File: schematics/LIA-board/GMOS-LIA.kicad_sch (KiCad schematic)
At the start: 0 parts

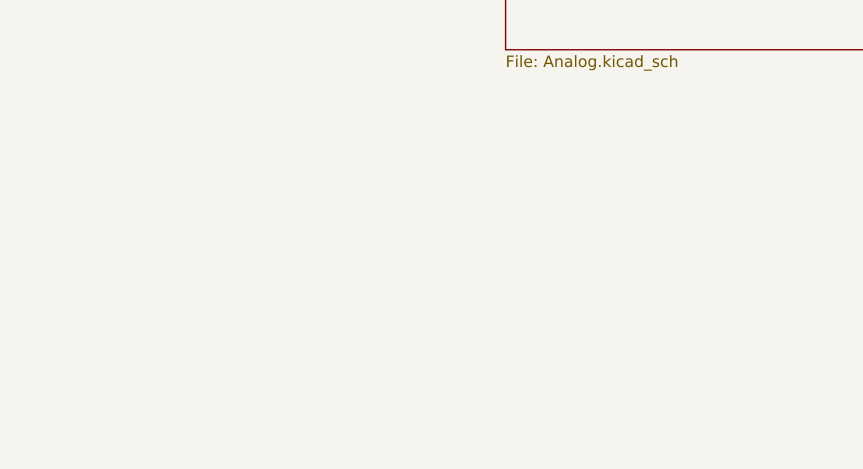
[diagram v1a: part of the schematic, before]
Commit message: some simulations, new page in kicad scematic
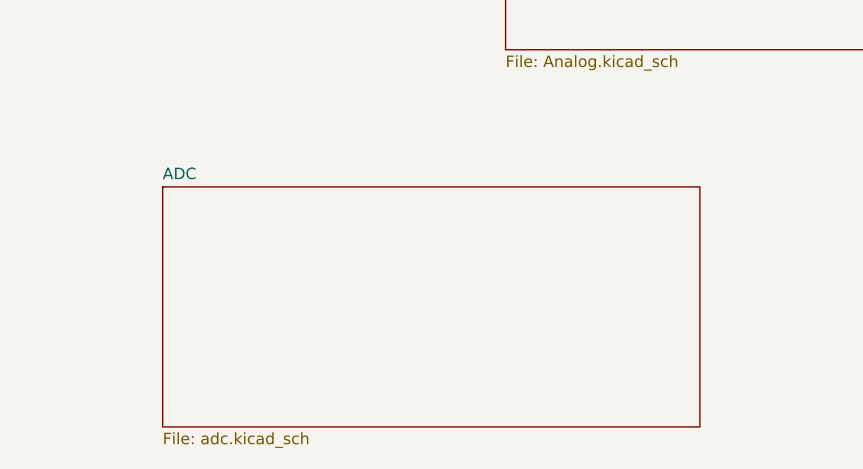
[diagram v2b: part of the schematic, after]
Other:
- added sheet ADC (adc.kicad_sch)
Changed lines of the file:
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@@
+		)
+	)
+	(sheet
+		(at 114.3 116.84)
+		(size 59.69 26.67)
+		(exclude_from_sim no)
+		(in_bom yes)
+		(on_board yes)
+		(dnp no)
+		(fields_autoplaced yes)
+		(stroke
+			(width 0.1524)
+			(type solid)
+		)
+		(fill
+			(color 0 0 0 0)
+		)
+		(property "Sheetname" "ADC"
+			(at 114.3 116.1284 0)
+			(show_name no)
+			(do_not_autoplace no)
+			(effects
+				(font
+					(size 1.27 1.27)
+				)
+				(justify left bottom)
+			)
+		)
+		(property "Sheetfile" "adc.kicad_sch"
+			(at 114.3 144.0946 0)
+			(show_name no)
+			(do_not_autoplace no)
+			(effects
+				(font
+					(size 1.27 1.27)
+				)
+				(justify left top)
+			)
+		)
+		(instances
+			(project "GMOS-LIA"
+				(path "/87b3d1ed-39bd-4cff-a405-e580c48ff0ef"
+					(page "7")
+				)
+			)
 		)
 	)

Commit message: all current changes
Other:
- sheet GMOS_Sock renamed GMOS_MUX
- sheet GMOS_MUX: file GMOS_Sock.kicad_sch -> GMOS_MUX.kicad_sch
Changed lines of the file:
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@@
 			(color 0 0 0 0)
 		)
-		(property "Sheetname" "GMOS_Sock"
+		(property "Sheetname" "GMOS_MUX"
 			(at 38.1 75.4884 0)
 			(show_name no)
@@
 			)
 		)
-		(property "Sheetfile" "GMOS_Sock.kicad_sch"
+		(property "Sheetfile" "GMOS_MUX.kicad_sch"
 			(at 38.1 111.0746 0)
 			(show_name no)

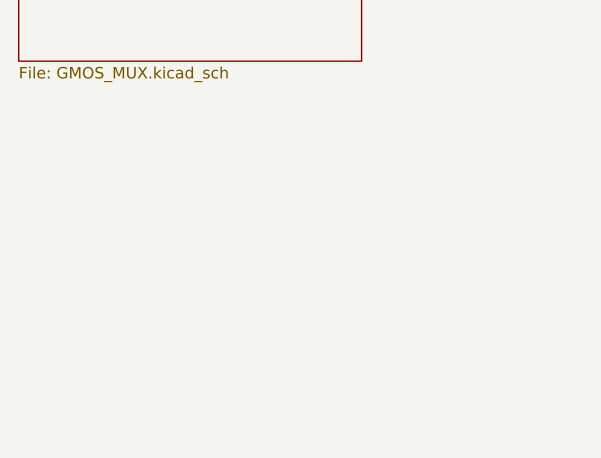
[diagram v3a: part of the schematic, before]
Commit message: added MCU
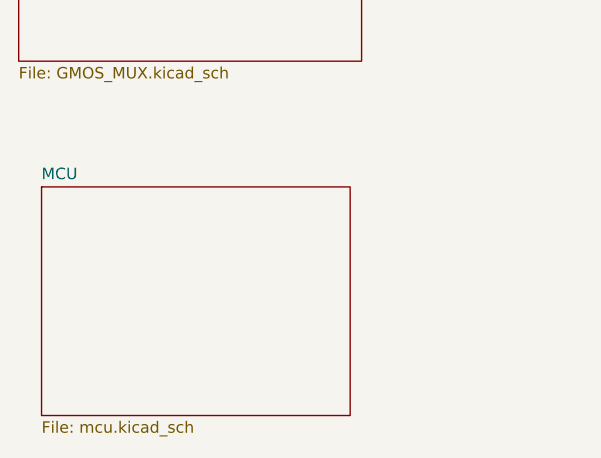
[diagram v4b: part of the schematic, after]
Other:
- added sheet MCU (mcu.kicad_sch)
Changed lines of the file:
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@@
+	)
+	(sheet
+		(at 40.64 124.46)
+		(size 34.29 25.4)
+		(exclude_from_sim no)
+		(in_bom yes)
+		(on_board yes)
+		(dnp no)
+		(fields_autoplaced yes)
+		(stroke
+			(width 0.1524)
+			(type solid)
+		)
+		(fill
+			(color 0 0 0 0)
+		)
+		(property "Sheetname" "MCU"
+			(at 40.64 123.7484 0)
+			(show_name no)
+			(do_not_autoplace no)
+			(effects
+				(font
+					(size 1.27 1.27)
+				)
+				(justify left bottom)
+			)
+		)
+		(property "Sheetfile" "mcu.kicad_sch"
+			(at 40.64 150.4446 0)
+			(show_name no)
+			(do_not_autoplace no)
+			(effects
+				(font
+					(size 1.27 1.27)
+				)
+				(justify left top)
+			)
+		)
+		(instances
+			(project "GMOS-LIA"
+				(path "/87b3d1ed-39bd-4cff-a405-e580c48ff0ef"
+					(page "8")
+				)
+			)
+		)
 	)
 	(sheet

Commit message: slight modifications to scenamtic
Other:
- added sheet DAC (DAC.kicad_sch)
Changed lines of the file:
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@@
 			(project "GMOS-LIA"
 				(path "/87b3d1ed-39bd-4cff-a405-e580c48ff0ef"
-					(page "8")
+					(page "9")
 				)
 			)
@@
 	)
 	(sheet
+		(at 99.06 115.57)
+		(size 55.88 27.94)
+		(exclude_from_sim no)
+		(in_bom yes)
+		(on_board yes)
+		(dnp no)
+		(fields_autoplaced yes)
+		(stroke
+			(width 0.1524)
+			(type solid)
+		)
+		(fill
+			(color 0 0 0 0)
+		)
+		(property "Sheetname" "DAC"
+			(at 99.06 114.8584 0)
+			(show_name no)
+			(do_not_autoplace no)
+			(effects
+				(font
+					(size 1.27 1.27)
+				)
+				(justify left bottom)
+			)
+		)
+		(property "Sheetfile" "DAC.kicad_sch"
+			(at 99.06 144.0946 0)
+			(show_name no)
+			(do_not_autoplace no)
+			(effects
+				(font
+					(size 1.27 1.27)
+				)
+				(justify left top)
+			)
+		)
+		(instances
+			(project "GMOS-LIA"
+				(path "/87b3d1ed-39bd-4cff-a405-e580c48ff0ef"
+					(page "8")
+				)
+			)
+		)
+	)
+	(sheet
 		(at 38.1 25.4)
 		(size 38.1 38.1)
@@
 	)
 	(sheet
-		(at 114.3 116.84)
+		(at 185.42 115.57)
 		(size 59.69 26.67)
 		(exclude_from_sim no)
@@
 		)
 		(property "Sheetname" "ADC"
-			(at 114.3 116.1284 0)
+			(at 185.42 114.8584 0)
 			(show_name no)
 			(do_not_autoplace no)
@@
 		)
 		(property "Sheetfile" "adc.kicad_sch"
-			(at 114.3 144.0946 0)
+			(at 185.42 142.8246 0)
 			(show_name no)
 			(do_not_autoplace no)

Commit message: modified scematic
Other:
- sheet DAC: file DAC.kicad_sch -> dac.kicad_sch
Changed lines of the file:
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@@
 			)
 		)
-		(property "Sheetfile" "DAC.kicad_sch"
+		(property "Sheetfile" "dac.kicad_sch"
 			(at 99.06 144.0946 0)
 			(show_name no)

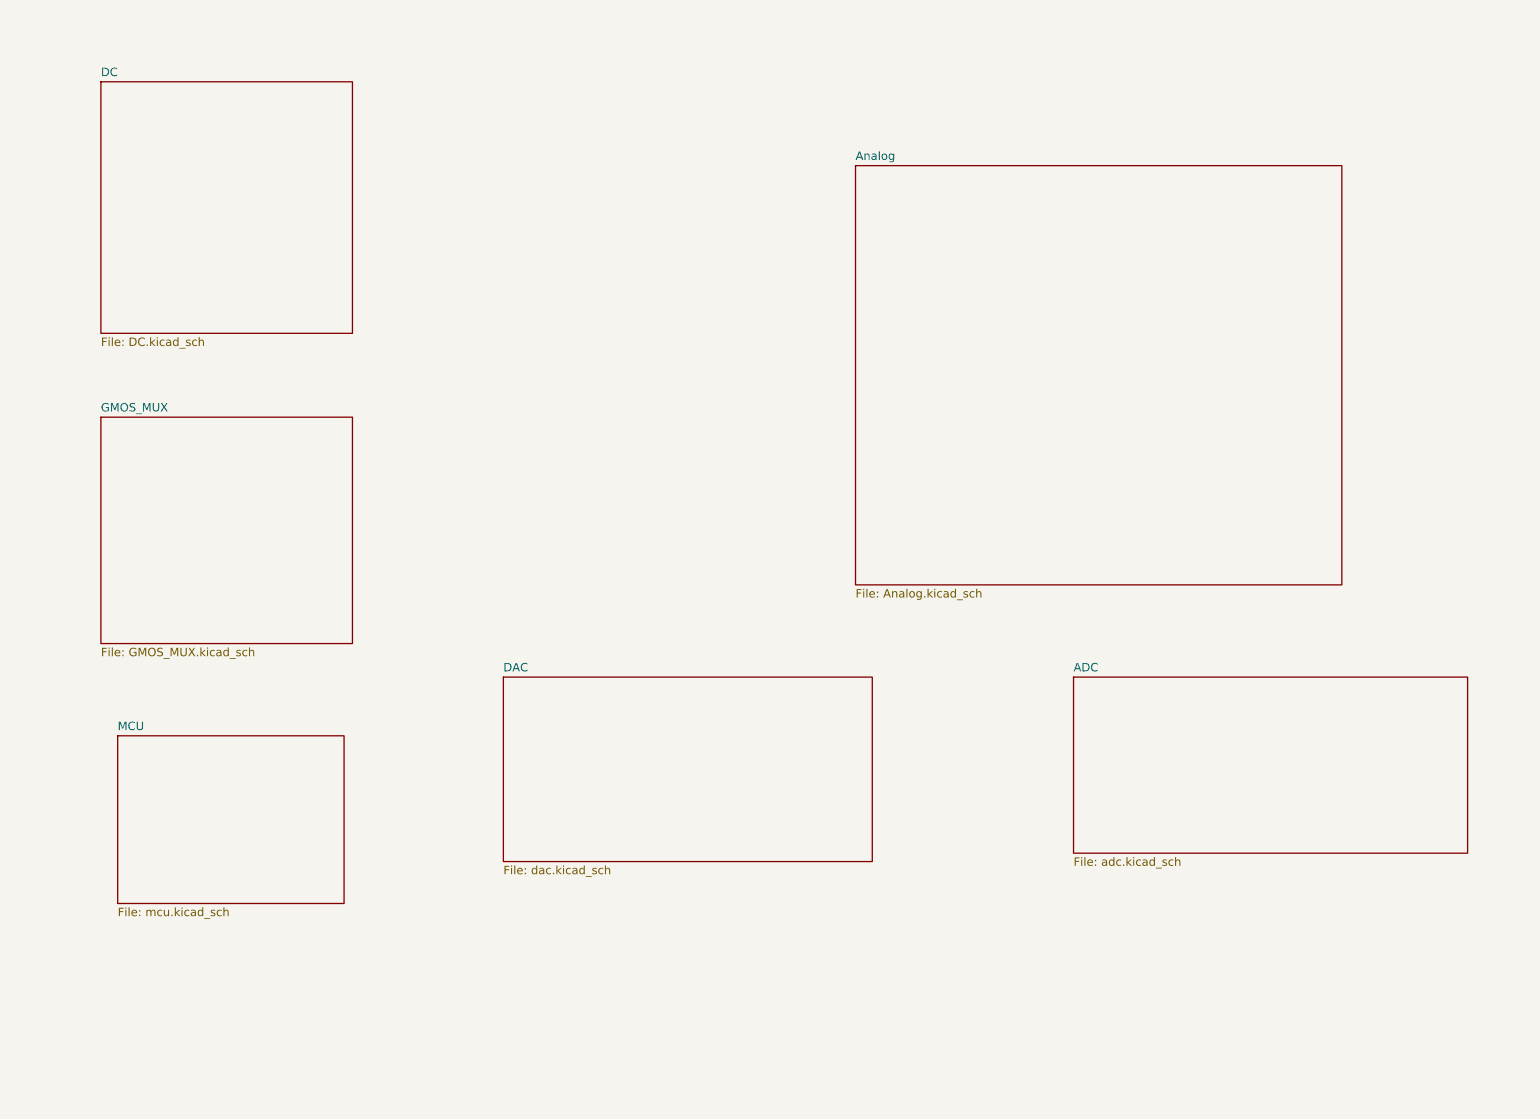
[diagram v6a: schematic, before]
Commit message: commit before changing the oscillator implementation
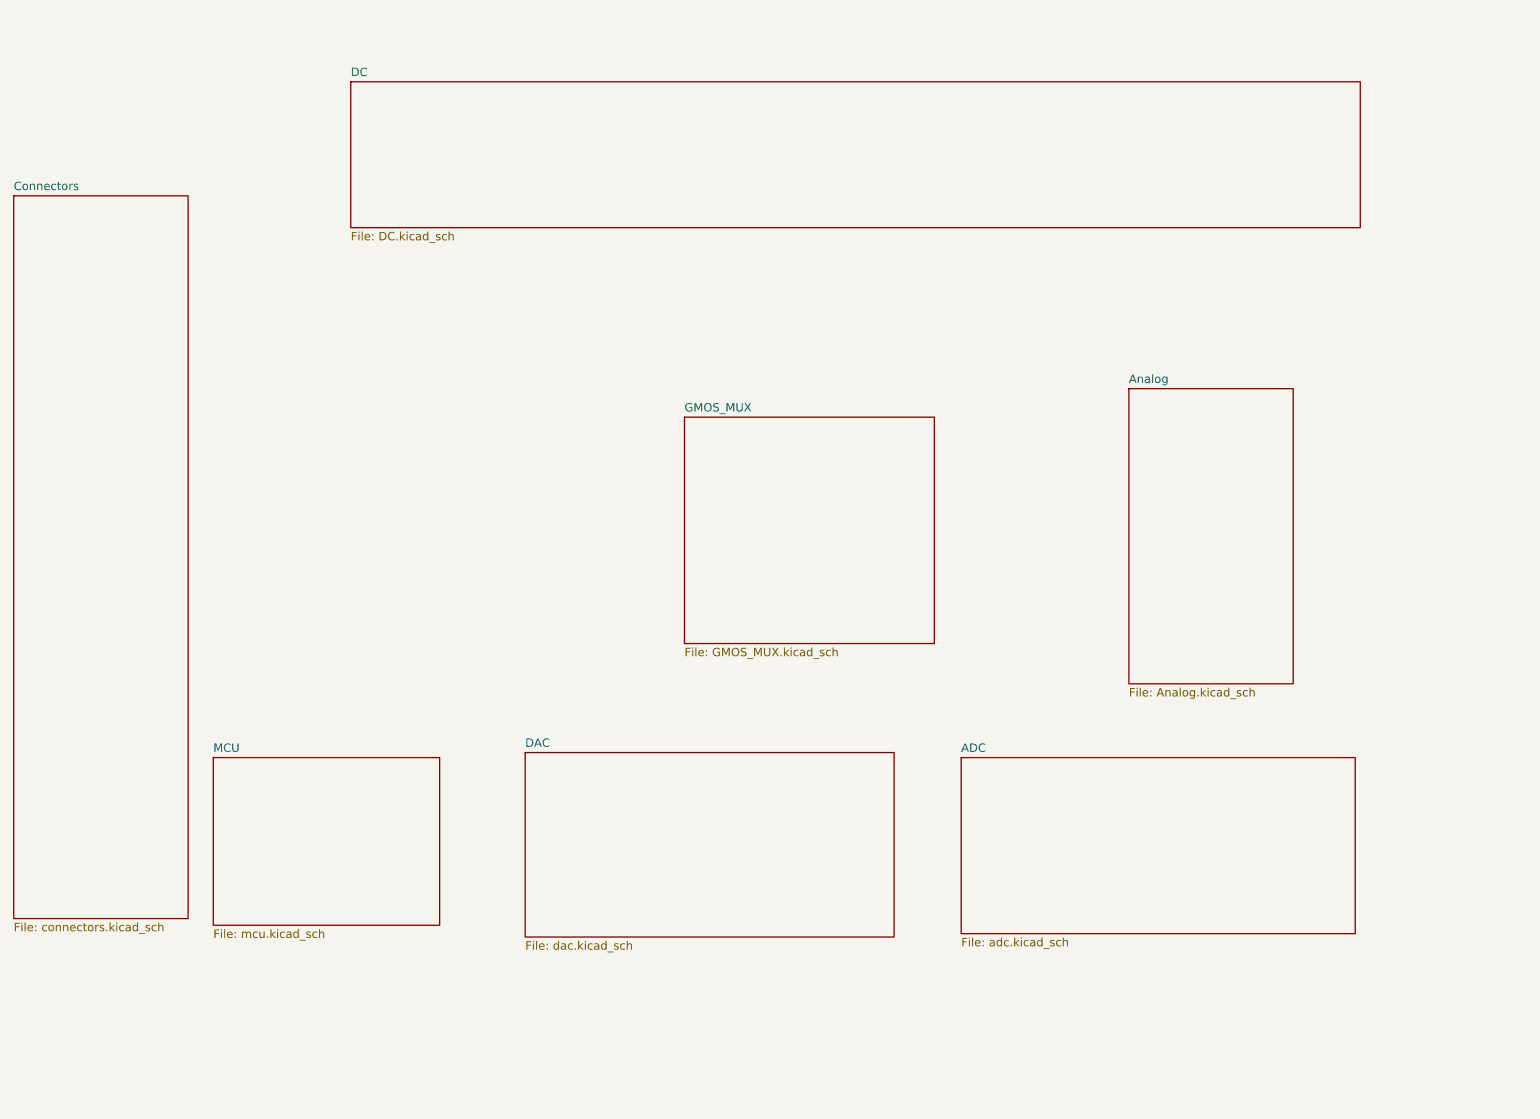
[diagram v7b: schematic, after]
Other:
- added sheet Connectors (connectors.kicad_sch)
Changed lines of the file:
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@@
 	(paper "A4")
 	(sheet
-		(at 152.4 38.1)
-		(size 73.66 63.5)
+		(at 193.802 71.882)
+		(size 24.892 44.704)
 		(exclude_from_sim no)
 		(in_bom yes)
@@
 		)
 		(property "Sheetname" "Analog"
-			(at 152.4 37.3884 0)
+			(at 193.802 71.1704 0)
 			(show_name no)
 			(do_not_autoplace no)
@@
 		)
 		(property "Sheetfile" "Analog.kicad_sch"
-			(at 152.4 102.1846 0)
+			(at 193.802 117.1706 0)
 			(show_name no)
 			(do_not_autoplace no)
@@
 	)
 	(sheet
-		(at 40.64 124.46)
+		(at 55.118 127.762)
 		(size 34.29 25.4)
 		(exclude_from_sim no)
@@
 		)
 		(property "Sheetname" "MCU"
-			(at 40.64 123.7484 0)
+			(at 55.118 127.0504 0)
 			(show_name no)
 			(do_not_autoplace no)
@@
 		)
 		(property "Sheetfile" "mcu.kicad_sch"
-			(at 40.64 150.4446 0)
+			(at 55.118 153.7466 0)
 			(show_name no)
 			(do_not_autoplace no)
@@
 	)
 	(sheet
-		(at 38.1 76.2)
-		(size 38.1 34.29)
+		(at 126.492 76.2)
+		(size 37.846 34.29)
 		(exclude_from_sim no)
 		(in_bom yes)
@@
 		)
 		(property "Sheetname" "GMOS_MUX"
-			(at 38.1 75.4884 0)
+			(at 126.492 75.4884 0)
 			(show_name no)
 			(do_not_autoplace no)
@@
 		)
 		(property "Sheetfile" "GMOS_MUX.kicad_sch"
-			(at 38.1 111.0746 0)
+			(at 126.492 111.0746 0)
 			(show_name no)
 			(do_not_autoplace no)
@@
 	)
 	(sheet
-		(at 99.06 115.57)
+		(at 102.362 127)
 		(size 55.88 27.94)
 		(exclude_from_sim no)
@@
 		)
 		(property "Sheetname" "DAC"
-			(at 99.06 114.8584 0)
+			(at 102.362 126.2884 0)
 			(show_name no)
 			(do_not_autoplace no)
@@
 		)
 		(property "Sheetfile" "dac.kicad_sch"
-			(at 99.06 144.0946 0)
+			(at 102.362 155.5246 0)
 			(show_name no)
 			(do_not_autoplace no)
@@
 	)
 	(sheet
-		(at 38.1 25.4)
-		(size 38.1 38.1)
+		(at 75.946 25.4)
+		(size 152.908 22.098)
 		(exclude_from_sim no)
 		(in_bom yes)
@@
 		)
 		(property "Sheetname" "DC"
-			(at 38.1 24.6884 0)
+			(at 75.946 24.6884 0)
 			(show_name no)
 			(do_not_autoplace no)
@@
 		)
 		(property "Sheetfile" "DC.kicad_sch"
-			(at 38.1 64.0846 0)
+			(at 75.946 48.0826 0)
 			(show_name no)
 			(do_not_autoplace no)
@@
 	)
 	(sheet
-		(at 185.42 115.57)
+		(at 24.892 42.672)
+		(size 26.416 109.474)
+		(exclude_from_sim no)
+		(in_bom yes)
+		(on_board yes)
+		(dnp no)
+		(fields_autoplaced yes)
+		(stroke
+			(width 0.1524)
+			(type solid)
+		)
+		(fill
+			(color 0 0 0 0)
+		)
+		(property "Sheetname" "Connectors"
+			(at 24.892 41.9604 0)
+			(show_name no)
+			(do_not_autoplace no)
+			(effects
+				(font
+					(size 1.27 1.27)
+				)
+				(justify left bottom)
+			)
+		)
+		(property "Sheetfile" "connectors.kicad_sch"
+			(at 24.892 152.7306 0)
+			(show_name no)
+			(do_not_autoplace no)
+			(effects
+				(font
+					(size 1.27 1.27)
+				)
+				(justify left top)
+			)
+		)
+		(instances
+			(project "GMOS-LIA"
+				(path "/87b3d1ed-39bd-4cff-a405-e580c48ff0ef"
+					(page "12")
+				)
+			)
+		)
+	)
+	(sheet
+		(at 168.402 127.762)
 		(size 59.69 26.67)
 		(exclude_from_sim no)
@@
 		)
 		(property "Sheetname" "ADC"
-			(at 185.42 114.8584 0)
+			(at 168.402 127.0504 0)
 			(show_name no)
 			(do_not_autoplace no)
@@
 		)
 		(property "Sheetfile" "adc.kicad_sch"
-			(at 185.42 142.8246 0)
-			(show_name no)
-			(do_not_autoplace no)
+			(at 168.402 155.0166 0)
+			(show_name no)
+			(do_not_autoplace no)

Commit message: commit before changing LIA
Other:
- removed sheet GMOS_MUX
- sheet ADC ports: added adc_cs, spi_clk, spi_miso, spi_mosi; removed none
- sheet Analog ports: added Vdrain_active, Vdrain_blind, Vheater_active, Vheater_blind, X_chop, X_readout, X_sync, Y_chop, Y_readout, Y_sync, ch_sel_[0..3], ext0_vadj, ext1_vadj, mcu_sin_ref, mux_en; removed none
- sheet Connectors ports: added Vcc_FTDI, Vin, iso_gnd, mcu_rst, swclk_in, swdio_in, uart_rx_iso, uart_tx_iso, usb_cc1, usb_cc2; removed none
- sheet DAC ports: added GMOS_Imeas[0..1], GMOS_Vadj[0..5], dac_cs, spi_clk, spi_miso, spi_mosi; removed none
- sheet DC ports: added 3V3_iso, 5V_FTDI, FTDI_gnd, Vin, i2c_scl, i2c_sda, usb_cc1, usb_cc2, usb_dp_rst; removed none
- sheet MCU ports: added V_imeas[0..1], iso_gnd, iso_vcc, mcu_i2c_scl, mcu_i2c_sda, mcu_sin_ref, msu_rst, spi_miso, spi_mosi, spi_sck, swclk, swdio, uart_rx_iso, uart_tx_iso; removed none
